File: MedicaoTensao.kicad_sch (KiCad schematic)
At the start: 20 parts, among them J4 Conn_01x02, J5 Conn_01x02, J6 Conn_01x02, U3 LM324

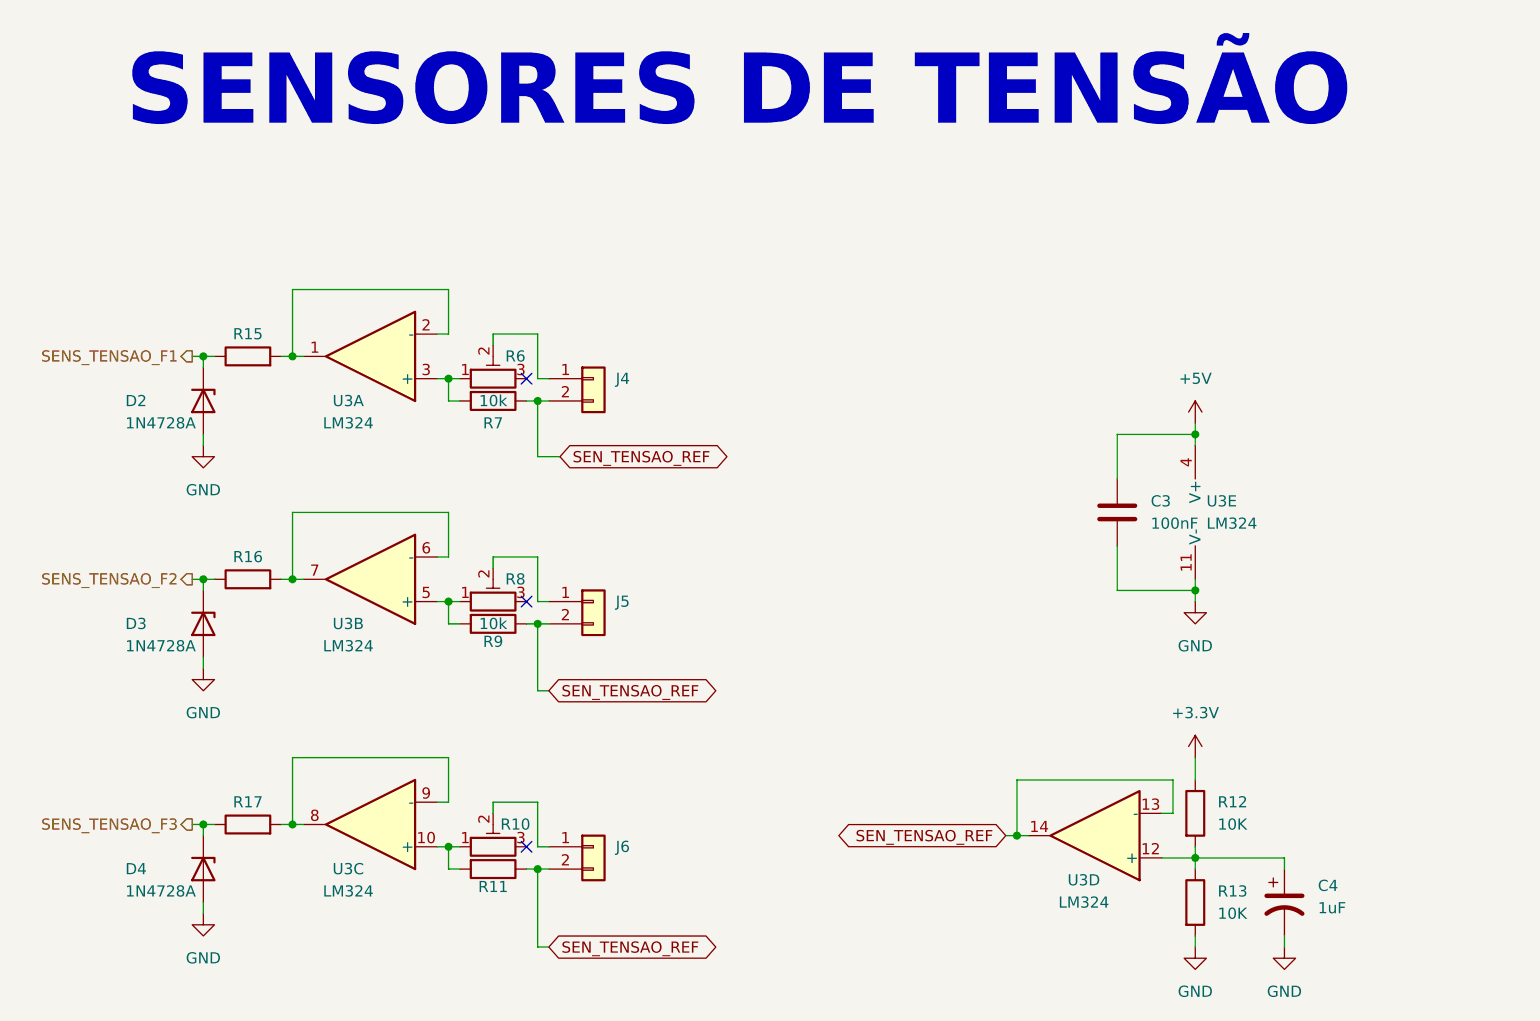
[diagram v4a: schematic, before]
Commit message: PCB e modelo 3D foram completados. As alterações necessárias foram feitas no esquemático para refletir o projeto desenvolvido na PCB. Teve-se que alterar o modelo do ESP32 para aquele que foi adquirido para o projeto.
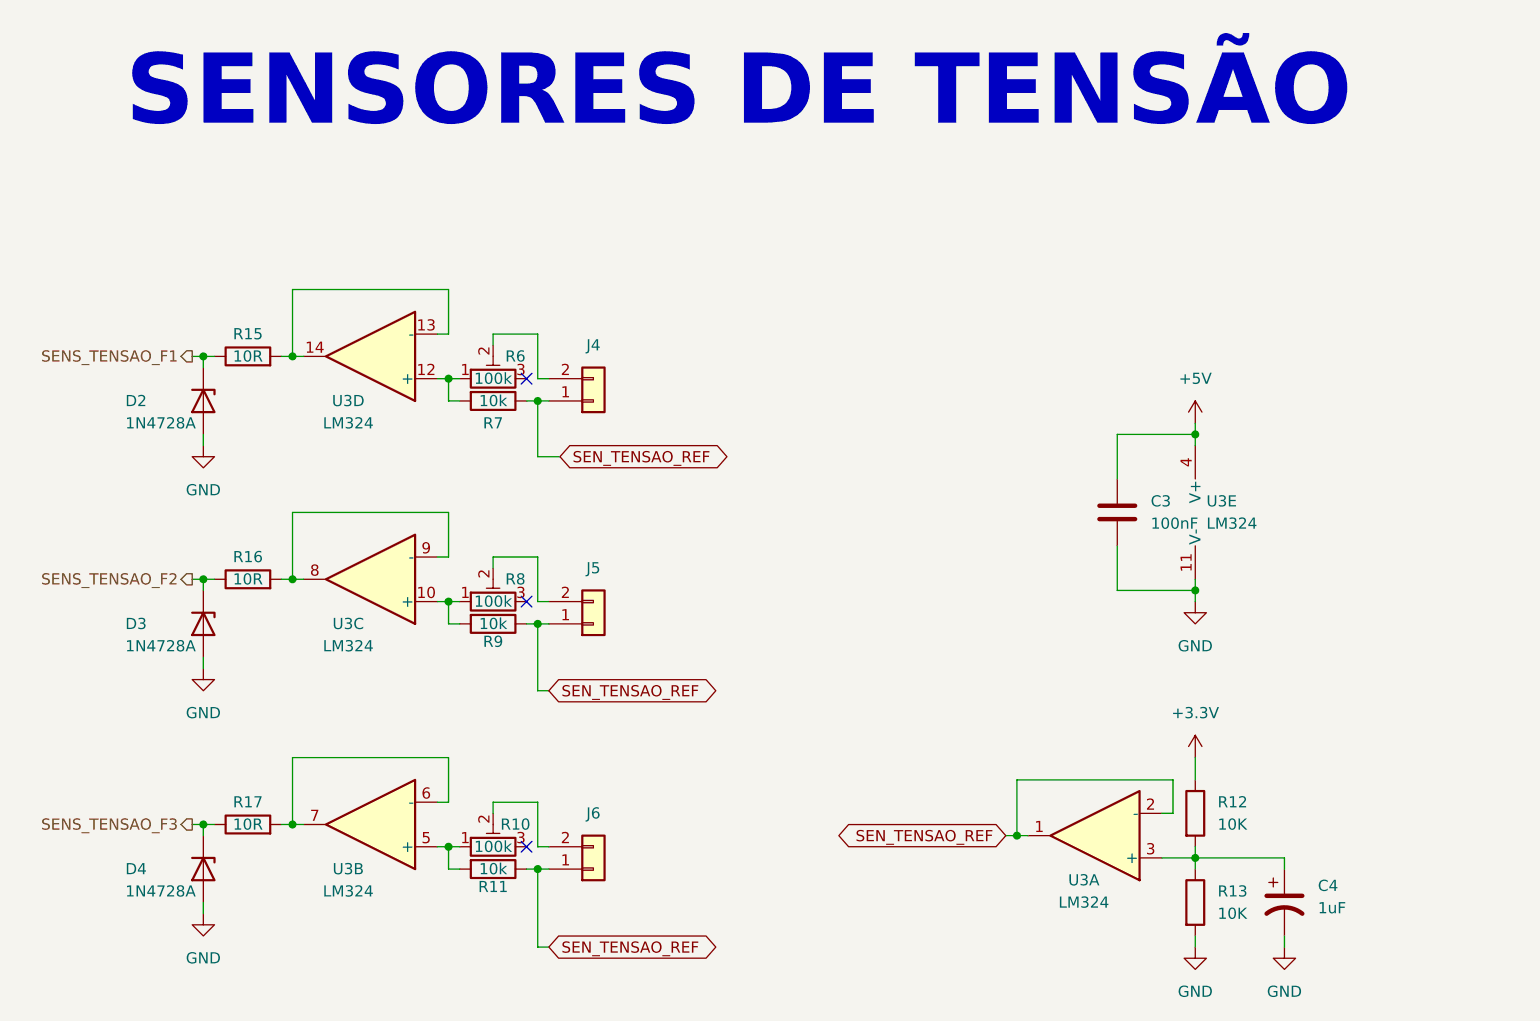
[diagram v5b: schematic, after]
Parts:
- R10, R6, R8: value (none) -> 100k; footprint (none) -> Potentiometer_THT:Potentiometer_Bourns_3296W_Vertical
- R11: value (none) -> 10k; footprint (none) -> Resistor_THT:R_Axial_DIN0207_L6.3mm_D2.5mm_P10.16mm_Horizontal
- R12, R13: footprint Resistor_THT:R_Axial_DIN0207_L6.3mm_D2.5mm_P10.16mm_Horizontal -> Resistor_THT:R_Axial_DIN0207_L6.3mm_D2.5mm_P2.54mm_Vertical
- R15, R16, R17: value (none) -> 10R; footprint (none) -> Resistor_THT:R_Axial_DIN0207_L6.3mm_D2.5mm_P2.54mm_Vertical
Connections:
- net SEN_TENSAO_REF: now also J4.1 (Pin_1), J5.1 (Pin_1), J6.1 (Pin_1), U3.1, U3.2 (-); no longer J4.2 (Pin_2), J5.2 (Pin_2), J6.2 (Pin_2), U3.13 (-), U3.14
- net at R6.1, R7.2: now also U3.12 (+); no longer U3.3 (+)
- net at R6.2: now also J4.2 (Pin_2); no longer J4.1 (Pin_1)
- net at R10.1, R11.2: now also U3.5 (+); no longer U3.10 (+)
- net at R8.1, R9.2: now also U3.10 (+); no longer U3.5 (+)
- net at C4.1, R12.2, R13.1: now also U3.3 (+); no longer U3.12 (+)
- net at R10.2: now also J6.2 (Pin_2); no longer J6.1 (Pin_1)
- net at R8.2: now also J5.2 (Pin_2); no longer J5.1 (Pin_1)
- new net: R17.2, U3.6 (-), U3.7
- new net: R16.2, U3.8, U3.9 (-)
- new net: R15.2, U3.13 (-), U3.14
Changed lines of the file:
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@@
     (in_bom yes) (on_board yes)
     (property "Reference" "R6" (id 0) (at 124.46 64.77 90))
-    (property "Value" "" (id 1) (at 121.92 67.31 90))
-    (property "Footprint" "" (id 2) (at 121.92 67.31 0)
+    (property "Value" "100k" (id 1) (at 121.92 67.31 90))
+    (property "Footprint" "Potentiometer_THT:Potentiometer_Bourns_3296W_Vertical" (id 2) (at 121.92 67.31 0)
       (effects (font (size 1.27 1.27)) hide)
     )
@@
     (pin "3")
   )
-  (symbol (lib_id "Amplifier_Operational:LM324") (at 107.95 118.11 180) (unit 3)
+  (symbol (lib_id "Amplifier_Operational:LM324") (at 107.95 118.11 180) (unit 2)
     (in_bom yes) (on_board yes)
     (property "Reference" "U3" (id 0) (at 105.41 123.19 0))
@@
     (in_bom yes) (on_board yes)
     (property "Reference" "R11" (id 0) (at 121.92 125.222 90))
-    (property "Value" "" (id 1) (at 121.92 123.19 90))
-    (property "Footprint" "" (id 2) (at 121.92 121.412 90)
+    (property "Value" "10k" (id 1) (at 121.92 123.19 90))
+    (property "Footprint" "Resistor_THT:R_Axial_DIN0207_L6.3mm_D2.5mm_P10.16mm_Horizontal" (id 2) (at 121.92 121.412 90)
       (effects (font (size 1.27 1.27)) hide)
     )
@@
     (in_bom yes) (on_board yes)
     (property "Reference" "R16" (id 0) (at 93.98 87.63 90))
-    (property "Value" "" (id 1) (at 93.98 90.17 90))
-    (property "Footprint" "" (id 2) (at 93.98 91.948 90)
+    (property "Value" "10R" (id 1) (at 93.98 90.17 90))
+    (property "Footprint" "Resistor_THT:R_Axial_DIN0207_L6.3mm_D2.5mm_P2.54mm_Vertical" (id 2) (at 93.98 91.948 90)
       (effects (font (size 1.27 1.27)) hide)
     )
@@
     (pin "2")
   )
-  (symbol (lib_id "Amplifier_Operational:LM324") (at 107.95 90.17 180) (unit 2)
+  (symbol (lib_id "Amplifier_Operational:LM324") (at 107.95 90.17 180) (unit 3)
     (in_bom yes) (on_board yes)
     (property "Reference" "U3" (id 0) (at 105.41 95.25 0))
@@
     (pin "4")
   )
-  (symbol (lib_id "Amplifier_Operational:LM324") (at 107.95 64.77 180) (unit 1)
+  (symbol (lib_id "Amplifier_Operational:LM324") (at 107.95 64.77 180) (unit 4)
     (in_bom yes) (on_board yes)
     (property "Reference" "U3" (id 0) (at 105.41 69.85 0))
@@
     (in_bom yes) (on_board yes)
     (property "Reference" "R17" (id 0) (at 93.98 115.57 90))
-    (property "Value" "" (id 1) (at 93.98 118.11 90))
-    (property "Footprint" "" (id 2) (at 93.98 119.888 90)
+    (property "Value" "10R" (id 1) (at 93.98 118.11 90))
+    (property "Footprint" "Resistor_THT:R_Axial_DIN0207_L6.3mm_D2.5mm_P2.54mm_Vertical" (id 2) (at 93.98 119.888 90)
       (effects (font (size 1.27 1.27)) hide)
     )
@@
     (pin "2")
   )
-  (symbol (lib_id "Connector_Generic:Conn_01x02") (at 133.35 67.31 0) (unit 1)
-    (in_bom yes) (on_board yes) (fields_autoplaced)
-    (property "Reference" "J4" (id 0) (at 135.89 67.3099 0)
-      (effects (font (size 1.27 1.27)) (justify left))
-    )
-    (property "Value" "Conn_01x02" (id 1) (at 135.89 69.8499 0)
+  (symbol (lib_id "Connector_Generic:Conn_01x02") (at 133.35 69.85 0) (mirror x) (unit 1)
+    (in_bom yes) (on_board yes) (fields_autoplaced)
+    (property "Reference" "J4" (id 0) (at 133.35 63.5 0))
+    (property "Value" "Conn_01x02" (id 1) (at 135.89 67.3101 0)
       (effects (font (size 1.27 1.27)) (justify left) hide)
     )
-    (property "Footprint" "TerminalBlock:TerminalBlock_bornier-2_P5.08mm" (id 2) (at 133.35 67.31 0)
-      (effects (font (size 1.27 1.27)) hide)
-    )
-    (property "Datasheet" "~" (id 3) (at 133.35 67.31 0)
+    (property "Footprint" "TerminalBlock:TerminalBlock_bornier-2_P5.08mm" (id 2) (at 133.35 69.85 0)
+      (effects (font (size 1.27 1.27)) hide)
+    )
+    (property "Datasheet" "~" (id 3) (at 133.35 69.85 0)
       (effects (font (size 1.27 1.27)) hide)
     )
@@
       (effects (font (size 1.27 1.27)) (justify left))
     )
-    (property "Footprint" "Resistor_THT:R_Axial_DIN0207_L6.3mm_D2.5mm_P10.16mm_Horizontal" (id 2) (at 200.152 127 90)
+    (property "Footprint" "Resistor_THT:R_Axial_DIN0207_L6.3mm_D2.5mm_P2.54mm_Vertical" (id 2) (at 200.152 127 90)
       (effects (font (size 1.27 1.27)) hide)
     )
@@
       (effects (font (size 1.27 1.27)) (justify left))
     )
-    (property "Footprint" "Resistor_THT:R_Axial_DIN0207_L6.3mm_D2.5mm_P10.16mm_Horizontal" (id 2) (at 200.152 116.84 90)
+    (property "Footprint" "Resistor_THT:R_Axial_DIN0207_L6.3mm_D2.5mm_P2.54mm_Vertical" (id 2) (at 200.152 116.84 90)
       (effects (font (size 1.27 1.27)) hide)
     )
@@
     (pin "1")
   )
-  (symbol (lib_id "Connector_Generic:Conn_01x02") (at 133.35 120.65 0) (unit 1)
-    (in_bom yes) (on_board yes) (fields_autoplaced)
-    (property "Reference" "J6" (id 0) (at 135.89 120.6499 0)
-      (effects (font (size 1.27 1.27)) (justify left))
-    )
-    (property "Value" "Conn_01x02" (id 1) (at 135.89 123.1899 0)
+  (symbol (lib_id "Connector_Generic:Conn_01x02") (at 133.35 123.19 0) (mirror x) (unit 1)
+    (in_bom yes) (on_board yes) (fields_autoplaced)
+    (property "Reference" "J6" (id 0) (at 133.35 116.84 0))
+    (property "Value" "Conn_01x02" (id 1) (at 135.89 120.6501 0)
       (effects (font (size 1.27 1.27)) (justify left) hide)
     )
-    (property "Footprint" "TerminalBlock:TerminalBlock_bornier-2_P5.08mm" (id 2) (at 133.35 120.65 0)
-      (effects (font (size 1.27 1.27)) hide)
-    )
-    (property "Datasheet" "~" (id 3) (at 133.35 120.65 0)
+    (property "Footprint" "TerminalBlock:TerminalBlock_bornier-2_P5.08mm" (id 2) (at 133.35 123.19 0)
+      (effects (font (size 1.27 1.27)) hide)
+    )
+    (property "Datasheet" "~" (id 3) (at 133.35 123.19 0)
       (effects (font (size 1.27 1.27)) hide)
     )
@@
     (in_bom yes) (on_board yes)
     (property "Reference" "R8" (id 0) (at 124.46 90.17 90))
-    (property "Value" "" (id 1) (at 121.92 92.71 90))
-    (property "Footprint" "" (id 2) (at 121.92 92.71 0)
+    (property "Value" "100k" (id 1) (at 121.92 92.71 90))
+    (property "Footprint" "Potentiometer_THT:Potentiometer_Bourns_3296W_Vertical" (id 2) (at 121.92 92.71 0)
       (effects (font (size 1.27 1.27)) hide)
     )
@@
     (in_bom yes) (on_board yes)
     (property "Reference" "R10" (id 0) (at 124.46 118.11 90))
-    (property "Value" "" (id 1) (at 121.92 120.65 90))
-    (property "Footprint" "" (id 2) (at 121.92 120.65 0)
+    (property "Value" "100k" (id 1) (at 121.92 120.65 90))
+    (property "Footprint" "Potentiometer_THT:Potentiometer_Bourns_3296W_Vertical" (id 2) (at 121.92 120.65 0)
       (effects (font (size 1.27 1.27)) hide)
     )
@@
     (pin "3")
   )
-  (symbol (lib_id "Amplifier_Operational:LM324") (at 190.5 119.38 180) (unit 4)
+  (symbol (lib_id "Amplifier_Operational:LM324") (at 190.5 119.38 180) (unit 1)
     (in_bom yes) (on_board yes)
     (property "Reference" "U3" (id 0) (at 189.23 124.46 0))
@@
     (in_bom yes) (on_board yes)
     (property "Reference" "R15" (id 0) (at 93.98 62.23 90))
-    (property "Value" "" (id 1) (at 93.98 64.77 90))
-    (property "Footprint" "" (id 2) (at 93.98 66.548 90)
+    (property "Value" "10R" (id 1) (at 93.98 64.77 90))
+    (property "Footprint" "Resistor_THT:R_Axial_DIN0207_L6.3mm_D2.5mm_P2.54mm_Vertical" (id 2) (at 93.98 66.548 90)
       (effects (font (size 1.27 1.27)) hide)
     )
@@
     (pin "2")
   )
-  (symbol (lib_id "Connector_Generic:Conn_01x02") (at 133.35 92.71 0) (unit 1)
-    (in_bom yes) (on_board yes) (fields_autoplaced)
-    (property "Reference" "J5" (id 0) (at 135.89 92.7099 0)
-      (effects (font (size 1.27 1.27)) (justify left))
-    )
-    (property "Value" "Conn_01x02" (id 1) (at 135.89 95.2499 0)
+  (symbol (lib_id "Connector_Generic:Conn_01x02") (at 133.35 95.25 0) (mirror x) (unit 1)
+    (in_bom yes) (on_board yes) (fields_autoplaced)
+    (property "Reference" "J5" (id 0) (at 133.35 88.9 0))
+    (property "Value" "Conn_01x02" (id 1) (at 135.89 92.7101 0)
       (effects (font (size 1.27 1.27)) (justify left) hide)
     )
-    (property "Footprint" "TerminalBlock:TerminalBlock_bornier-2_P5.08mm" (id 2) (at 133.35 92.71 0)
-      (effects (font (size 1.27 1.27)) hide)
-    )
-    (property "Datasheet" "~" (id 3) (at 133.35 92.71 0)
-      (effects (font (size 1.27 1.27)) hide)
-    )
+    (property "Footprint" "TerminalBlock:TerminalBlock_bornier-2_P5.08mm" (id 2) (at 133.35 95.25 0)
+      (effects (font (size 1.27 1.27)) hide)
+    )
+    (property "Datasheet" "~" (id 3) (at 133.35 95.25 0)
+      (effects (font (size 1.27 1.27)) hide)
+    )
